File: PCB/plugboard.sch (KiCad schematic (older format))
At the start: 121 parts, among them J1 1/4\" Jack, J10 Conn_01x19_Male_0, J11 Conn_01x19_Male_0, J2 1/4\" Jack, J3 1/4\" Jack, J4 1/4\" Jack, J5 1/4\" Jack, J6 1/4\" Jack, J7 1/4\" Jack, J8 1/4\" Jack, J9 1/4\" Jack, P1 CONN_02X03, P2 CONN_02X03, U1 ADG732

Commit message: Basic Layout
Now I'm gonna start on tracing.
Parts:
- removed R? (x26): R_10K, enigmaprints:R_0805_OEM, symbol formula:R_10K
- added R45: R_10K, enigmaprints:R_0805_OEM, symbol formula:R_10K
- C1: footprint footprints:C_0805_OEM -> enigmaprints:R_0805_OEM
- U1: footprint footprints:48-TQFP -> enigmaprints:ADG732BSUZ-REEL
- renumbered J9 to J10, J4 to J2, J7 to J3, J2 to J4, J8 to J6, J10 to J7, J3 to J8, J6 to J9, R12 to R10, R13 to R11, R14 to R12, R25 to R13, R32 to R14, R33 to R15, R40 to R16, R53 to R17, R54 to R18, R61 to R19, R68 to R20, R75 to R21, R76 to R22, R77 to R23, R78 to R24, R79 to R25, R80 to R26, R15 to R27, R19 to R28, R26 to R29, R34 to R30, R41 to R31, R47 to R32, R55 to R33, R62 to R34, R69 to R35, R16 to R36, R20 to R37, R27 to R38, R35 to R39, R42 to R40, R48 to R41, R56 to R42, R63 to R43, R70 to R44, R21 to R46, R28 to R47, R36 to R48, R43 to R49, R49 to R50, R57 to R51, R64 to R52, R71 to R53, R22 to R54, R29 to R55, R37 to R56, R44 to R57, R50 to R58, R58 to R59, R65 to R60, R72 to R61, R17 to R62, R23 to R63, R30 to R64, R38 to R65, R45 to R66, R51 to R67, R59 to R68, R66 to R69, R73 to R70, R18 to R71, R24 to R72, R31 to R73, R39 to R74, R46 to R75, R52 to R76, R60 to R77, R67 to R78, R74 to R79, R9 to R80, R11 to R81, R10 to R9
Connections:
- net Dout: now also R45.1
- net GND: now also R45.2
- net VCC: now also R48.1
- net S1 renamed SQ
- net S10 renamed SR
- net S11 renamed ST
- net S12 renamed SZ
- net S13 renamed SF
- net S14 renamed SG
- net S15 renamed SC
- net S16 renamed SV
- net S17 renamed SB
- net S18 renamed SH
- net S19 renamed SU
- net S2 renamed SW
- net S20 renamed SI
- net S21 renamed SO
- net S22 renamed SJ
- net S23 renamed SK
- net S24 renamed SN
- net S25 renamed SM
- net S26 renamed SL
- net S3 renamed SE
- net S4 renamed SA
- net S5 renamed SS
- net S6 renamed SP
- net S7 renamed SY
- net S8 renamed SX
- net S9 renamed SD
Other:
- moved on the sheet: J1, J10, J11, J2, J3, J4, J5, J6, J7, J8, J9, R27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

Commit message: update schematic
I'm gonna try something...
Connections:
- net B: now also R24.1, R25.2; no longer R1.1, R2.2
- net C: now also R6.1, R7.2; no longer R2.1, R3.2
- net E: now also R17.1, R18.2; no longer R4.1, R5.2
- net F: now also R12.1, R13.2; no longer R5.1, R6.2
- net G: now also R21.1, R22.2; no longer R6.1, R7.2
- net H: now also R4.1, R5.2; no longer R7.1, R8.2
- net I: now also R10.1, R11.2; no longer R8.1, R9.2
- net J: now also R13.1, R14.2; no longer R10.2, R9.1
- net K: now also R22.1, R23.2; no longer R10.1, R11.2
- net L: now also R25.1, R26.2; no longer R11.1, R12.2
- net M: now also R16.1, R17.2; no longer R12.1, R13.2
- net N: now also R7.1, R8.2; no longer R13.1, R14.2
- net O: now also R19.1, R20.2; no longer R14.1, R15.2
- net P: now also R5.1, R6.2; no longer R15.1, R16.2
- net R: now also R1.1, R2.2; no longer R17.1, R18.2
- net S: now also R20.1, R21.2; no longer R18.1, R19.2
- net SA: now also U1.36 (S28); no longer U1.9 (S4)
- net SB: now also U1.5 (S8); no longer U1.25 (S17)
- net SC: now also U1.31 (S23); no longer U1.46 (S15)
- net SD: now also U1.28 (S20); no longer U1.4 (S9)
- net SE: now also U1.46 (S15); no longer U1.10 (S3)
- net SF: now also U1.37 (S29); no longer U1.48 (S13)
- net SG: now also U1.2 (S11); no longer U1.47 (S14)
- net SH: now also U1.29 (S21); no longer U1.26 (S18)
- net SI: now also U1.35 (S27); no longer U1.28 (S20)
- net SJ: now also U1.38 (S30); no longer U1.30 (S22)
- net SK: now also U1.3 (S10); no longer U1.31 (S23)
- net SL: now also U1.6 (S7); no longer U1.34 (S26)
- net SM: now also U1.45 (S16); no longer U1.33 (S25)
- net SO: now also U1.48 (S13); no longer U1.29 (S21)
- net SP: now also U1.30 (S22); no longer U1.7 (S6)
- net SQ: now also U1.25 (S17); no longer U1.12 (S1)
- net SR: now also U1.26 (S18); no longer U1.3 (S10)
- net SS: now also U1.1 (S12); no longer U1.8 (S5)
- net ST: now also U1.34 (S26); no longer U1.2 (S11)
- net SV: now also U1.40 (S32); no longer U1.45 (S16)
- net SW: now also U1.33 (S25); no longer U1.11 (S2)
- net SX: now also U1.4 (S9); no longer U1.5 (S8)
- net SY: now also U1.39 (S31); no longer U1.6 (S7)
- net SZ: now also U1.47 (S14); no longer U1.1 (S12)
- net T: now also R10.2, R9.1; no longer R19.1, R20.2
- net U: now also R2.1, R3.2; no longer R20.1, R21.2
- net V: now also R15.1, R16.2; no longer R21.1, R22.2
- net VCC: now also R27.2; no longer R48.1
- net W: now also R8.1, R9.2; no longer R22.1, R23.2
- net Y: now also R14.1, R15.2; no longer R24.1, R25.2
- net Z: now also R18.1, R19.2; no longer R25.1, R26.2
- removed net Q: R16.1, R17.2, R27.2
- new net A: R11.1, R12.2, R48.1
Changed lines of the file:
@@
 	550  900  750  900
 Text Label 650  900  0    50   ~ 0
-A
+Q
 Text Label 1100 900  0    50   ~ 0
-B
+R
 Wire Wire Line
 	1050 900  1150 900
@@
 	1550 900  1450 900
 Text Label 1500 900  0    50   ~ 0
-C
+U
 Text Label 1900 900  0    50   ~ 0
 D
 Text Label 2300 900  0    50   ~ 0
-E
+H
 Text Label 2700 900  0    50   ~ 0
-F
+P
 Text Label 3100 900  0    50   ~ 0
-G
+C
 Text Label 3500 900  0    50   ~ 0
-H
+N
 Wire Wire Line
 	3550 900  3450 900
 Text Label 3900 900  0    50   ~ 0
+W
+Text Label 4300 900  0    50   ~ 0
+T
+Text Label 4700 900  0    50   ~ 0
 I
-Text Label 4300 900  0    50   ~ 0
+Text Label 5100 900  0    50   ~ 0
+A
+Text Label 5500 900  0    50   ~ 0
+F
+Text Label 5900 900  0    50   ~ 0
 J
-Text Label 4700 900  0    50   ~ 0
+Text Label 6300 900  0    50   ~ 0
+Y
+Text Label 6700 900  0    50   ~ 0
+V
+Text Label 7100 900  0    50   ~ 0
+M
+Text Label 7500 900  0    50   ~ 0
+E
+Text Label 7900 900  0    50   ~ 0
+Z
+Text Label 8300 900  0    50   ~ 0
+O
+Text Label 8700 900  0    50   ~ 0
+S
+Text Label 9100 900  0    50   ~ 0
+G
+Text Label 9500 900  0    50   ~ 0
 K
-Text Label 5100 900  0    50   ~ 0
-L
-Text Label 5500 900  0    50   ~ 0
-M
-Text Label 5900 900  0    50   ~ 0
-N
-Text Label 6300 900  0    50   ~ 0
-O
-Text Label 6700 900  0    50   ~ 0
-P
-Text Label 7100 900  0    50   ~ 0
-Q
-Text Label 7500 900  0    50   ~ 0
-R
-Text Label 7900 900  0    50   ~ 0
-S
-Text Label 8300 900  0    50   ~ 0
-T
-Text Label 8700 900  0    50   ~ 0
-U
-Text Label 9100 900  0    50   ~ 0
-V
-Text Label 9500 900  0    50   ~ 0
-W
 Text Label 9900 900  0    50   ~ 0
 X
 Text Label 10300 900  0    50   ~ 0
-Y
+B
 $Comp
 L formula:R_1K R25
@@
 $EndComp
 Text Label 10700 900  0    50   ~ 0
-Z
+L
 Wire Wire Line
 	2050 2100 2150 2100
@@
 Text Label 6550 2950 3    50   ~ 0
 SW
-Text Label 1500 5250 2    50   ~ 0
+Text Label 3300 4200 1    50   ~ 0
 SY
+Text Label 1500 4950 2    50   ~ 0
+SX
+Text Label 4050 5700 0    50   ~ 0
+SD
+Text Label 4050 6000 0    50   ~ 0
+SR
+Text Label 4050 5250 0    50   ~ 0
+SC
+Text Label 3150 4200 1    50   ~ 0
+SV
 Text Label 1500 5100 2    50   ~ 0
-SX
-Text Label 1500 4950 2    50   ~ 0
-SD
-Text Label 1500 4800 2    50   ~ 0
-SR
-Text Label 2250 4200 1    50   ~ 0
-SC
-Text Label 2400 4200 1    50   ~ 0
-SV
-Text Label 4050 6150 0    50   ~ 0
 SB
-Text Label 4050 6000 0    50   ~ 0
+Text Label 4050 5550 0    50   ~ 0
 SH
 Text Label 4050 5850 0    50   ~ 0
 SU
-Text Label 4050 5700 0    50   ~ 0
+Text Label 4050 4650 0    50   ~ 0
 SI
-Text Label 4050 5550 0    50   ~ 0
+Text Label 1950 4200 1    50   ~ 0
 SO
-Text Label 4050 5400 0    50   ~ 0
+Text Label 3450 4200 1    50   ~ 0
 SJ
-Text Label 4050 4800 0    50   ~ 0
+Text Label 1500 5250 2    50   ~ 0
 SL
 Text Label 4050 5100 0    50   ~ 0
 SN
-Text Label 4050 5250 0    50   ~ 0
+Text Label 1500 4800 2    50   ~ 0
 SK
-Text Label 1500 5850 2    50   ~ 0
+Text Label 2250 4200 1    50   ~ 0
 SE
-Text Label 1500 5700 2    50   ~ 0
+Text Label 4050 4500 0    50   ~ 0
 SA
-Text Label 1500 5550 2    50   ~ 0
+Text Label 1500 4500 2    50   ~ 0
 SS
-Text Label 1500 5400 2    50   ~ 0
+Text Label 4050 5400 0    50   ~ 0
 SP
+Text Label 4050 4800 0    50   ~ 0
+ST
+Text Label 2100 4200 1    50   ~ 0
+SZ
+Text Label 3600 4200 1    50   ~ 0
+SF
 Text Label 1500 4650 2    50   ~ 0
-ST
-Text Label 1500 4500 2    50   ~ 0
-SZ
-Text Label 1950 4200 1    50   ~ 0
-SF
-Text Label 2100 4200 1    50   ~ 0
 SG
-Text Label 4050 4950 0    50   ~ 0
+Text Label 2400 4200 1    50   ~ 0
 SM
 Text Label 6550 5100 3    50   ~ 0
@@
 Text Label 5200 5100 3    50   ~ 0
 SP
-Text Label 1500 6150 2    50   ~ 0
+Text Label 4050 6150 0    50   ~ 0
 SQ
-Text Label 1500 6000 2    50   ~ 0
+Text Label 4050 4950 0    50   ~ 0
 SW
-NoConn ~ 4050 4500
-NoConn ~ 4050 4650
-NoConn ~ 3600 4200
-NoConn ~ 3450 4200
-NoConn ~ 3300 4200
-NoConn ~ 3150 4200
 NoConn ~ 3000 4200
 NoConn ~ 2850 4200
@@
 	1    0    0    -1
 $EndComp
+NoConn ~ 1500 5400
+NoConn ~ 1500 5550
+NoConn ~ 1500 5700
+NoConn ~ 1500 5850
+NoConn ~ 1500 6000
+NoConn ~ 1500 6150
 $EndSCHEMATC

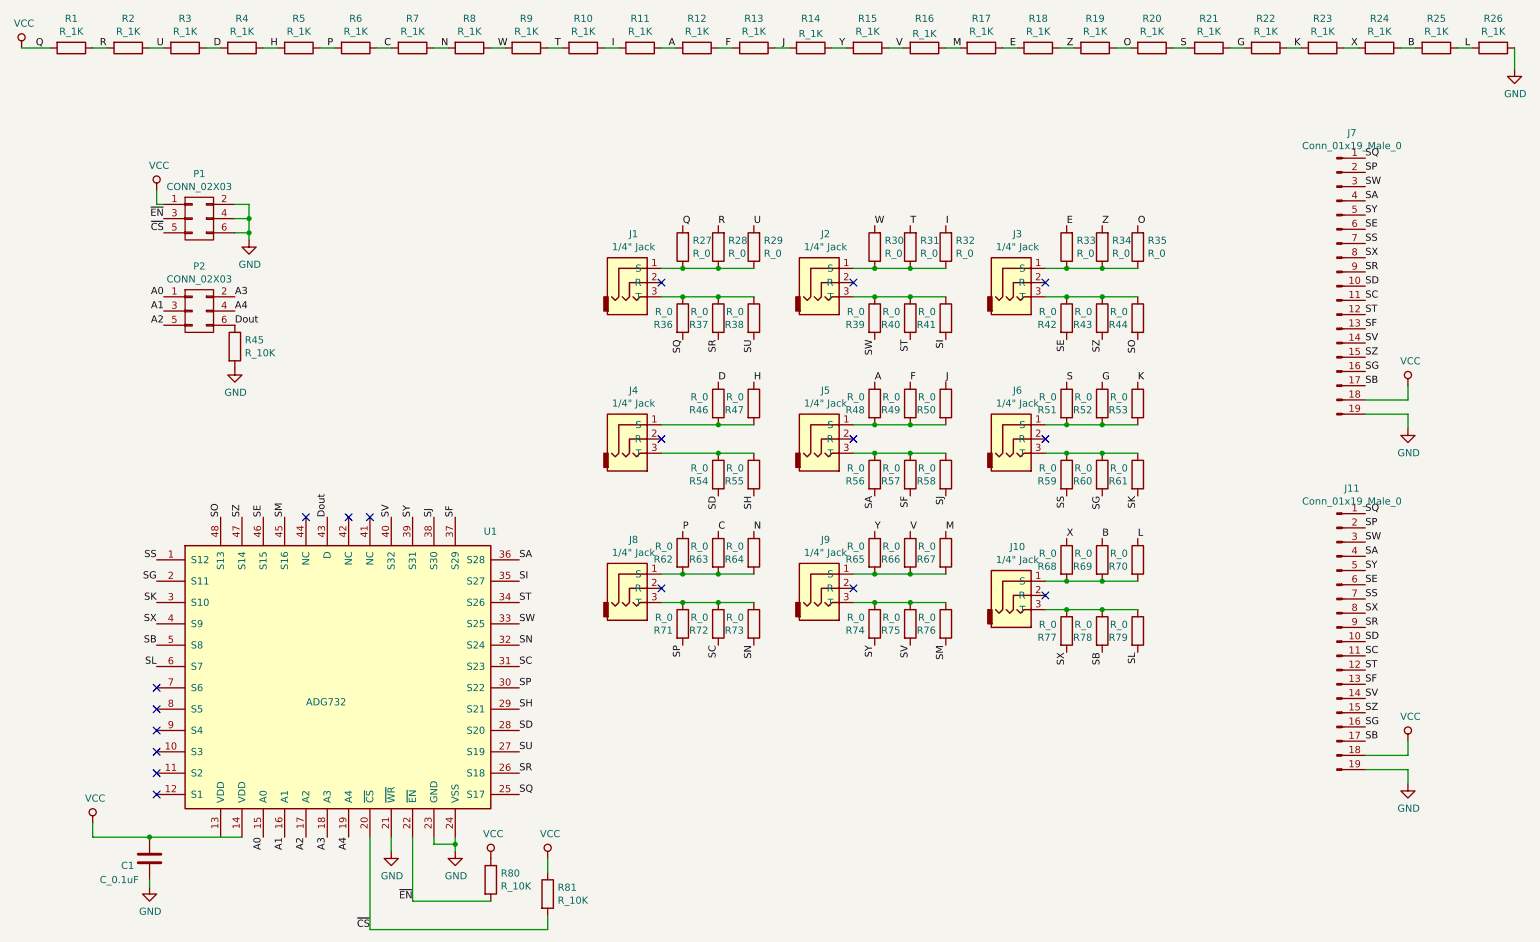
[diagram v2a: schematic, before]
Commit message: Layout work
It's working!
I did a few optimization changes to make layout smoother.
Changed around the netlist essentially
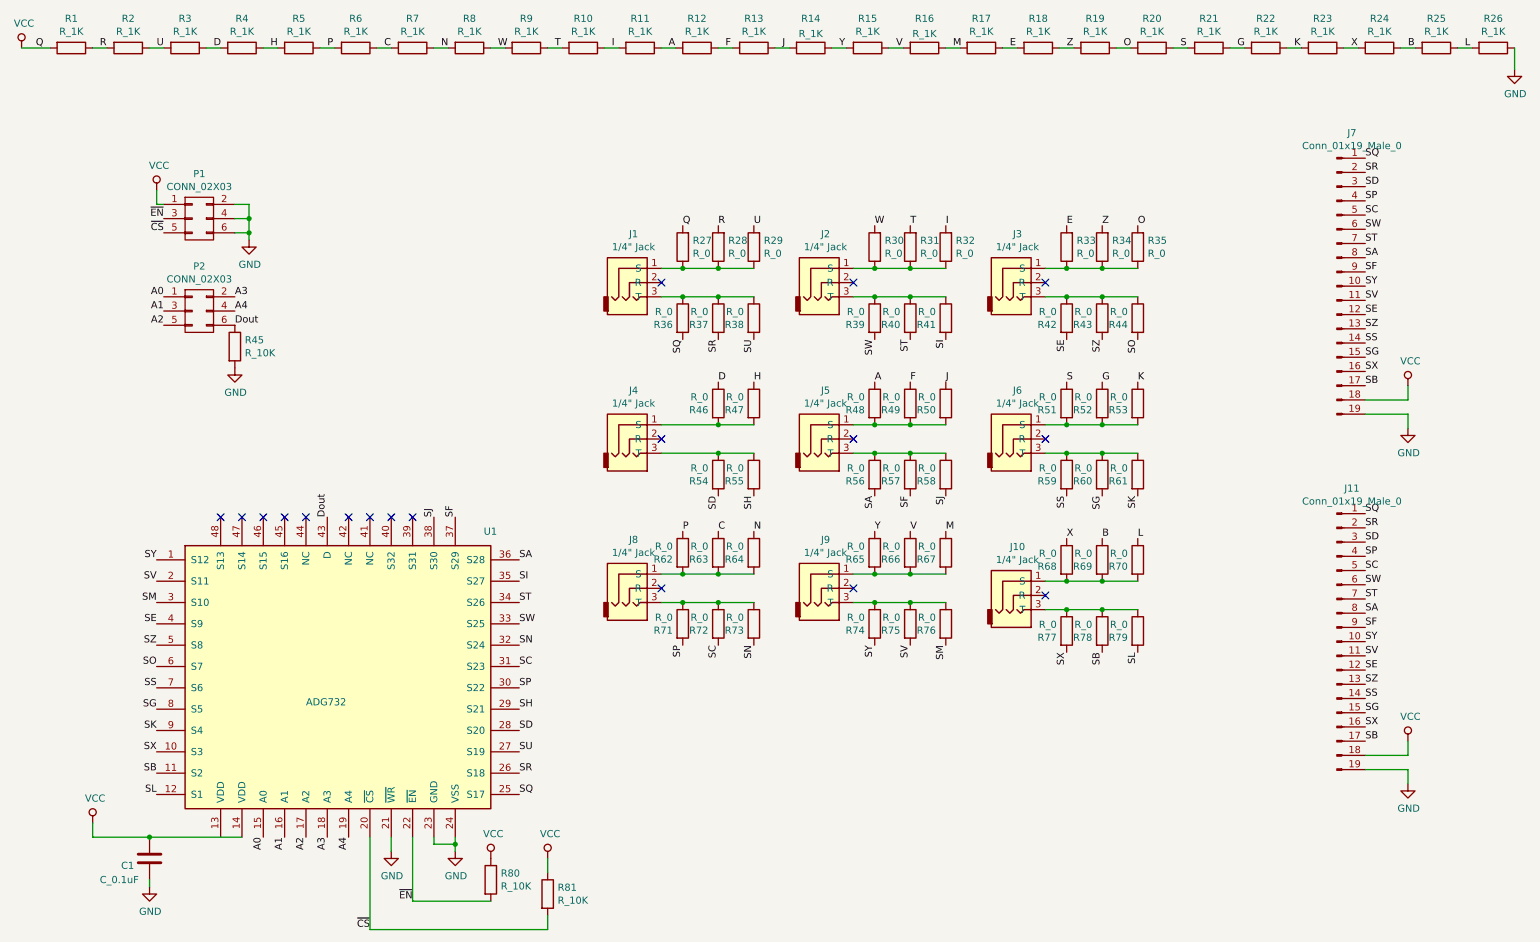
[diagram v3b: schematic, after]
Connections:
- net SA: now also J11.8 (Pin_8), J7.8 (Pin_8); no longer J11.4 (Pin_4), J7.4 (Pin_4)
- net SB: now also U1.11 (S2); no longer U1.5 (S8)
- net SC: now also J11.5 (Pin_5), J7.5 (Pin_5); no longer J11.11 (Pin_11), J7.11 (Pin_11)
- net SD: now also J11.3 (Pin_3), J7.3 (Pin_3); no longer J11.10 (Pin_10), J7.10 (Pin_10)
- net SE: now also J11.12 (Pin_12), J7.12 (Pin_12), U1.4 (S9); no longer J11.6 (Pin_6), J7.6 (Pin_6), U1.46 (S15)
- net SF: now also J11.9 (Pin_9), J7.9 (Pin_9); no longer J11.13 (Pin_13), J7.13 (Pin_13)
- net SG: now also J11.15 (Pin_15), J7.15 (Pin_15), U1.8 (S5); no longer J11.16 (Pin_16), J7.16 (Pin_16), U1.2 (S11)
- net SK: now also U1.9 (S4); no longer U1.3 (S10)
- net SL: now also U1.12 (S1); no longer U1.6 (S7)
- net SM: now also U1.3 (S10); no longer U1.45 (S16)
- net SO: now also U1.6 (S7); no longer U1.48 (S13)
- net SP: now also J11.4 (Pin_4), J7.4 (Pin_4); no longer J11.2 (Pin_2), J7.2 (Pin_2)
- net SR: now also J11.2 (Pin_2), J7.2 (Pin_2); no longer J11.9 (Pin_9), J7.9 (Pin_9)
- net SS: now also J11.14 (Pin_14), J7.14 (Pin_14), U1.7 (S6); no longer J11.7 (Pin_7), J7.7 (Pin_7), U1.1 (S12)
- net ST: now also J11.7 (Pin_7), J7.7 (Pin_7); no longer J11.12 (Pin_12), J7.12 (Pin_12)
- net SV: now also J11.11 (Pin_11), J7.11 (Pin_11), U1.2 (S11); no longer J11.14 (Pin_14), J7.14 (Pin_14), U1.40 (S32)
- net SW: now also J11.6 (Pin_6), J7.6 (Pin_6); no longer J11.3 (Pin_3), J7.3 (Pin_3)
- net SX: now also J11.16 (Pin_16), J7.16 (Pin_16), U1.10 (S3); no longer J11.8 (Pin_8), J7.8 (Pin_8), U1.4 (S9)
- net SY: now also J11.10 (Pin_10), J7.10 (Pin_10), U1.1 (S12); no longer J11.5 (Pin_5), J7.5 (Pin_5), U1.39 (S31)
- net SZ: now also J11.13 (Pin_13), J7.13 (Pin_13), U1.5 (S8); no longer J11.15 (Pin_15), J7.15 (Pin_15), U1.47 (S14)
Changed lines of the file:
@@
 Text Label 6550 2950 3    50   ~ 0
 SW
-Text Label 3300 4200 1    50   ~ 0
+Text Label 1500 4500 2    50   ~ 0
 SY
-Text Label 1500 4950 2    50   ~ 0
+Text Label 1500 5850 2    50   ~ 0
 SX
 Text Label 4050 5700 0    50   ~ 0
@@
 Text Label 4050 5250 0    50   ~ 0
 SC
-Text Label 3150 4200 1    50   ~ 0
+Text Label 1500 4650 2    50   ~ 0
 SV
-Text Label 1500 5100 2    50   ~ 0
+Text Label 1500 6000 2    50   ~ 0
 SB
 Text Label 4050 5550 0    50   ~ 0
@@
 Text Label 4050 4650 0    50   ~ 0
 SI
-Text Label 1950 4200 1    50   ~ 0
+Text Label 1500 5250 2    50   ~ 0
 SO
 Text Label 3450 4200 1    50   ~ 0
 SJ
-Text Label 1500 5250 2    50   ~ 0
+Text Label 1500 6150 2    50   ~ 0
 SL
 Text Label 4050 5100 0    50   ~ 0
 SN
-Text Label 1500 4800 2    50   ~ 0
+Text Label 1500 5700 2    50   ~ 0
 SK
-Text Label 2250 4200 1    50   ~ 0
+Text Label 1500 4950 2    50   ~ 0
 SE
 Text Label 4050 4500 0    50   ~ 0
 SA
-Text Label 1500 4500 2    50   ~ 0
+Text Label 1500 5400 2    50   ~ 0
 SS
 Text Label 4050 5400 0    50   ~ 0
@@
 Text Label 4050 4800 0    50   ~ 0
 ST
-Text Label 2100 4200 1    50   ~ 0
+Text Label 1500 5100 2    50   ~ 0
 SZ
 Text Label 3600 4200 1    50   ~ 0
 SF
-Text Label 1500 4650 2    50   ~ 0
+Text Label 1500 5550 2    50   ~ 0
 SG
-Text Label 2400 4200 1    50   ~ 0
+Text Label 1500 4800 2    50   ~ 0
 SM
 Text Label 6550 5100 3    50   ~ 0
@@
 	1    0    0    -1
 $EndComp
-Text Label 10000 1675 0    50   ~ 0
+Text Label 10000 4175 0    50   ~ 0
 SQ
-Text Label 10000 1875 0    50   ~ 0
+Text Label 10000 4675 0    50   ~ 0
 SW
-Text Label 10000 2175 0    50   ~ 0
+Text Label 10000 5275 0    50   ~ 0
 SE
-Text Label 10000 1775 0    50   ~ 0
+Text Label 10000 4475 0    50   ~ 0
 SP
-Text Label 10000 2575 0    50   ~ 0
+Text Label 10000 4375 0    50   ~ 0
 SD
-Text Label 10000 2275 0    50   ~ 0
+Text Label 10000 5475 0    50   ~ 0
 SS
-Text Label 10000 1975 0    50   ~ 0
+Text Label 10000 4875 0    50   ~ 0
 SA
-Text Label 10000 2075 0    50   ~ 0
+Text Label 10000 5075 0    50   ~ 0
 SY
-Text Label 10000 2375 0    50   ~ 0
+Text Label 10000 5675 0    50   ~ 0
 SX
 $Comp
@@
 Text Label 5700 4050 3    50   ~ 0
 SH
-Text Label 10000 2475 0    50   ~ 0
+Text Label 10000 4275 0    50   ~ 0
 SR
-Text Label 10000 2675 0    50   ~ 0
+Text Label 10000 4575 0    50   ~ 0
 SC
-Text Label 10000 2775 0    50   ~ 0
+Text Label 10000 4775 0    50   ~ 0
 ST
-Text Label 10000 2875 0    50   ~ 0
+Text Label 10000 4975 0    50   ~ 0
 SF
-Text Label 10000 2975 0    50   ~ 0
+Text Label 10000 5175 0    50   ~ 0
 SV
-Text Label 10000 3075 0    50   ~ 0
+Text Label 10000 5375 0    50   ~ 0
 SZ
-Text Label 10000 3175 0    50   ~ 0
+Text Label 10000 5575 0    50   ~ 0
 SG
-Text Label 10000 3275 0    50   ~ 0
+Text Label 10000 5775 0    50   ~ 0
 SB
 $Comp
@@
 	1    0    0    -1
 $EndComp
-Text Label 10000 4175 0    50   ~ 0
-SQ
-Text Label 10000 4375 0    50   ~ 0
-SW
-Text Label 10000 4675 0    50   ~ 0
-SE
-Text Label 10000 4275 0    50   ~ 0
-SP
-Text Label 10000 5075 0    50   ~ 0
-SD
-Text Label 10000 4775 0    50   ~ 0
-SS
-Text Label 10000 4475 0    50   ~ 0
-SA
-Text Label 10000 4575 0    50   ~ 0
-SY
-Text Label 10000 4875 0    50   ~ 0
-SX
-Text Label 10000 4975 0    50   ~ 0
-SR
-Text Label 10000 5175 0    50   ~ 0
-SC
-Text Label 10000 5275 0    50   ~ 0
-ST
-Text Label 10000 5375 0    50   ~ 0
-SF
-Text Label 10000 5475 0    50   ~ 0
-SV
-Text Label 10000 5575 0    50   ~ 0
-SZ
-Text Label 10000 5675 0    50   ~ 0
-SG
-Text Label 10000 5775 0    50   ~ 0
-SB
 $Comp
 L power:VCC #PWR014
@@
 	1    0    0    -1
 $EndComp
-NoConn ~ 1500 5400
-NoConn ~ 1500 5550
-NoConn ~ 1500 5700
-NoConn ~ 1500 5850
-NoConn ~ 1500 6000
-NoConn ~ 1500 6150
+NoConn ~ 1950 4200
+NoConn ~ 2100 4200
+NoConn ~ 2250 4200
+NoConn ~ 2400 4200
+NoConn ~ 3150 4200
+NoConn ~ 3300 4200
+Text Label 10000 1675 0    50   ~ 0
+SQ
+Text Label 10000 2175 0    50   ~ 0
+SW
+Text Label 10000 2775 0    50   ~ 0
+SE
+Text Label 10000 1975 0    50   ~ 0
+SP
+Text Label 10000 1875 0    50   ~ 0
+SD
+Text Label 10000 2975 0    50   ~ 0
+SS
+Text Label 10000 2375 0    50   ~ 0
+SA
+Text Label 10000 2575 0    50   ~ 0
+SY
+Text Label 10000 3175 0    50   ~ 0
+SX
+Text Label 10000 1775 0    50   ~ 0
+SR
+Text Label 10000 2075 0    50   ~ 0
+SC
+Text Label 10000 2275 0    50   ~ 0
+ST
+Text Label 10000 2475 0    50   ~ 0
+SF
+Text Label 10000 2675 0    50   ~ 0
+SV
+Text Label 10000 2875 0    50   ~ 0
+SZ
+Text Label 10000 3075 0    50   ~ 0
+SG
+Text Label 10000 3275 0    50   ~ 0
+SB
 $EndSCHEMATC
